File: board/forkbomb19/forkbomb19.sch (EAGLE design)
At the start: 67 parts, among them T3 MMUN2133LT1G, U1 ESP-WROOM-03, U4 TPS61090RSAR, U5 MCP73871, X3 POT_GND, X4 POT_3V3, X5 POT_SIG

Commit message: performing board review
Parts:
- TOUCH: value TOUCHPAD -> TOUCHPADTOUCH_BLANK; device forkbomb19:TOUCHPAD -> forkbomb19:TOUCHPADTOUCH_BLANK
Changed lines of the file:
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@@
 <part name="GND21" library="supply1" library_urn="urn:adsk.eagle:library:371" deviceset="GND" device=""/>
 <part name="+3V13" library="supply1" library_urn="urn:adsk.eagle:library:371" deviceset="+3V3" device=""/>
-<part name="TOUCH" library="forkbomb19" deviceset="TOUCHPAD" device=""/>
+<part name="TOUCH" library="forkbomb19" deviceset="TOUCHPAD" device="TOUCH_BLANK" value="TOUCHPADTOUCH_BLANK"/>
 <part name="U4" library="microbuilder" deviceset="VREG_TPS6103X" device="" value="TPS61090RSAR"/>
 <part name="L1" library="microbuilder" deviceset="INDUCTOR" device="TDK_VLC5045" value="6.8uH"/>
@@
 <part name="U$19" library="microbuilder" deviceset="VBAT" device=""/>
 <part name="LOW_BATT" library="led" library_urn="urn:adsk.eagle:library:259" deviceset="LED" device="CHIP-LED0603" package3d_urn="urn:adsk.eagle:package:15819/3" value="RED"/>
-<part name="R20" library="rcl" library_urn="urn:adsk.eagle:library:334" deviceset="R-US_" device="R0603" package3d_urn="urn:adsk.eagle:package:23555/2" value="1K"/>
-<part name="R18" library="rcl" library_urn="urn:adsk.eagle:library:334" deviceset="R-US_" device="R0603" package3d_urn="urn:adsk.eagle:package:23555/2" value="200K"/>
+<part name="R20" library="rcl" library_urn="urn:adsk.eagle:library:334" deviceset="R-US_" device="R0603" package3d_urn="urn:adsk.eagle:package:23555/3" value="1K"/>
+<part name="R18" library="rcl" library_urn="urn:adsk.eagle:library:334" deviceset="R-US_" device="R0603" package3d_urn="urn:adsk.eagle:package:23555/3" value="200K"/>
 <part name="U$27" library="microbuilder" deviceset="VBAT" device=""/>
 <part name="U$24" library="microbuilder" deviceset="GND" device=""/>
 <part name="C16" library="rcl" library_urn="urn:adsk.eagle:library:334" deviceset="C-US" device="C0603" package3d_urn="urn:adsk.eagle:package:23616/2" value="100nF"/>
-<part name="R19" library="rcl" library_urn="urn:adsk.eagle:library:334" deviceset="R-US_" device="R0603" package3d_urn="urn:adsk.eagle:package:23555/2" value="1.12M"/>
-<part name="R21" library="rcl" library_urn="urn:adsk.eagle:library:334" deviceset="R-US_" device="R0603" package3d_urn="urn:adsk.eagle:package:23555/2" value="200K"/>
+<part name="R19" library="rcl" library_urn="urn:adsk.eagle:library:334" deviceset="R-US_" device="R0603" package3d_urn="urn:adsk.eagle:package:23555/3" value="1.12M"/>
+<part name="R21" library="rcl" library_urn="urn:adsk.eagle:library:334" deviceset="R-US_" device="R0603" package3d_urn="urn:adsk.eagle:package:23555/3" value="200K"/>
 <part name="U$9" library="microbuilder" deviceset="GND" device=""/>
 <part name="U$10" library="microbuilder" deviceset="GND" device=""/>
-<part name="R23" library="rcl" library_urn="urn:adsk.eagle:library:334" deviceset="R-US_" device="R0603" package3d_urn="urn:adsk.eagle:package:23555/2" value="340K"/>
-<part name="R24" library="rcl" library_urn="urn:adsk.eagle:library:334" deviceset="R-US_" device="R0603" package3d_urn="urn:adsk.eagle:package:23555/2" value="1.87M"/>
+<part name="R23" library="rcl" library_urn="urn:adsk.eagle:library:334" deviceset="R-US_" device="R0603" package3d_urn="urn:adsk.eagle:package:23555/3" value="340K"/>
+<part name="R24" library="rcl" library_urn="urn:adsk.eagle:library:334" deviceset="R-US_" device="R0603" package3d_urn="urn:adsk.eagle:package:23555/3" value="1.87M"/>
 <part name="U$20" library="microbuilder" deviceset="GND" device=""/>
 <part name="U$23" library="microbuilder" deviceset="VBAT" device=""/>
 <part name="T3" library="transistor" library_urn="urn:adsk.eagle:library:402" deviceset="*-PNP_DRIVER-" device="SC59-BEC" package3d_urn="urn:adsk.eagle:package:28754/2" technology="MUN2114T1" value="MMUN2133LT1G"/>
 <part name="GND22" library="supply1" deviceset="GND" device=""/>
-<part name="R25" library="rcl" library_urn="urn:adsk.eagle:library:334" deviceset="R-US_" device="R0603" package3d_urn="urn:adsk.eagle:package:23555/2" value="270K"/>
-<part name="R26" library="rcl" library_urn="urn:adsk.eagle:library:334" deviceset="R-US_" device="R0603" package3d_urn="urn:adsk.eagle:package:23555/2" value="100K"/>
+<part name="R25" library="rcl" library_urn="urn:adsk.eagle:library:334" deviceset="R-US_" device="R0603" package3d_urn="urn:adsk.eagle:package:23555/3" value="270K"/>
+<part name="R26" library="rcl" library_urn="urn:adsk.eagle:library:334" deviceset="R-US_" device="R0603" package3d_urn="urn:adsk.eagle:package:23555/3" value="100K"/>
 <part name="GND24" library="supply1" deviceset="GND" device=""/>
 <part name="DONE" library="led" library_urn="urn:adsk.eagle:library:259" deviceset="LED" device="CHIP-LED0603" package3d_urn="urn:adsk.eagle:package:15819/3" value="GREEN"/>
 <part name="CHRG" library="led" library_urn="urn:adsk.eagle:library:259" deviceset="LED" device="CHIP-LED0603" package3d_urn="urn:adsk.eagle:package:15819/3" value="ORANGE"/>
-<part name="R27" library="rcl" library_urn="urn:adsk.eagle:library:334" deviceset="R-US_" device="R0603" package3d_urn="urn:adsk.eagle:package:23555/2" value="1K"/>
-<part name="R28" library="rcl" library_urn="urn:adsk.eagle:library:334" deviceset="R-US_" device="R0603" package3d_urn="urn:adsk.eagle:package:23555/2" value="1K"/>
+<part name="R27" library="rcl" library_urn="urn:adsk.eagle:library:334" deviceset="R-US_" device="R0603" package3d_urn="urn:adsk.eagle:package:23555/3" value="1K"/>
+<part name="R28" library="rcl" library_urn="urn:adsk.eagle:library:334" deviceset="R-US_" device="R0603" package3d_urn="urn:adsk.eagle:package:23555/3" value="1K"/>
 <part name="GND25" library="supply1" deviceset="GND" device=""/>
-<part name="R29" library="rcl" library_urn="urn:adsk.eagle:library:334" deviceset="R-US_" device="R0603" package3d_urn="urn:adsk.eagle:package:23555/2" value="1.0K"/>
-<part name="R30" library="rcl" library_urn="urn:adsk.eagle:library:334" deviceset="R-US_" device="R0603" package3d_urn="urn:adsk.eagle:package:23555/2" value="100K"/>
+<part name="R29" library="rcl" library_urn="urn:adsk.eagle:library:334" deviceset="R-US_" device="R0603" package3d_urn="urn:adsk.eagle:package:23555/3" value="1.0K"/>
+<part name="R30" library="rcl" library_urn="urn:adsk.eagle:library:334" deviceset="R-US_" device="R0603" package3d_urn="urn:adsk.eagle:package:23555/3" value="100K"/>
 <part name="GND26" library="supply1" deviceset="GND" device=""/>
 <part name="GND27" library="supply1" deviceset="GND" device=""/>
 <part name="GND29" library="supply1" deviceset="GND" device=""/>
-<part name="THERM" library="rcl" library_urn="urn:adsk.eagle:library:334" deviceset="R-US_" device="R0603" package3d_urn="urn:adsk.eagle:package:23555/2" value="15K"/>
+<part name="THERM" library="rcl" library_urn="urn:adsk.eagle:library:334" deviceset="R-US_" device="R0603" package3d_urn="urn:adsk.eagle:package:23555/3" value="15K"/>
 <part name="U$34" library="microbuilder" deviceset="VBAT" device=""/>
 <part name="U$36" library="microbuilder" deviceset="VBUS" device=""/>
@@
 <part name="U5" library="microbuilder" deviceset="MCP73871" device="" value="MCP73871"/>
 <part name="+3V11" library="supply1" library_urn="urn:adsk.eagle:library:371" deviceset="+3V3" device=""/>
-<part name="R9" library="rcl" library_urn="urn:adsk.eagle:library:334" deviceset="R-US_" device="R0603" package3d_urn="urn:adsk.eagle:package:23555/2" value="200k"/>
+<part name="R9" library="rcl" library_urn="urn:adsk.eagle:library:334" deviceset="R-US_" device="R0603" package3d_urn="urn:adsk.eagle:package:23555/3" value="200k"/>
 <part name="U$1" library="microbuilder" deviceset="GND" device=""/>
-<part name="C10" library="rcl" library_urn="urn:adsk.eagle:library:334" deviceset="CPOL-US" device="C/6032-28R" package3d_urn="urn:adsk.eagle:package:23415/1" value="100uF"/>
+<part name="C10" library="rcl" library_urn="urn:adsk.eagle:library:334" deviceset="CPOL-US" device="C/6032-28R" package3d_urn="urn:adsk.eagle:package:23415/2" value="100uF"/>
 <part name="U$7" library="forkbomb19" deviceset="MLX90640" device=""/>
 <part name="+3V14" library="supply1" library_urn="urn:adsk.eagle:library:371" deviceset="+3V3" device=""/>
@@
 <instance part="C14" gate="G$1" x="-50.8" y="-114.3" smashed="yes" rot="MR0">
 <attribute name="NAME" x="-51.816" y="-113.665" size="1.778" layer="95" rot="MR0"/>
-<attribute name="VALUE" x="-49.276" y="-121.031" size="1.778" layer="96" rot="MR0"/>
+<attribute name="VALUE" x="-49.276" y="-118.491" size="1.778" layer="96" rot="MR0"/>
 </instance>
 <instance part="GND19" gate="1" x="-50.8" y="-127" smashed="yes">
@@
 </instance>
 <instance part="C10" gate="G$1" x="-78.74" y="-101.6" smashed="yes">
-<attribute name="NAME" x="-77.724" y="-100.965" size="1.778" layer="95"/>
-<attribute name="VALUE" x="-77.724" y="-105.791" size="1.778" layer="96"/>
+<attribute name="NAME" x="-85.344" y="-100.965" size="1.778" layer="95"/>
+<attribute name="VALUE" x="-85.344" y="-105.791" size="1.778" layer="96"/>
 </instance>
 <instance part="U$7" gate="G$1" x="60.96" y="-109.22" smashed="yes"/>

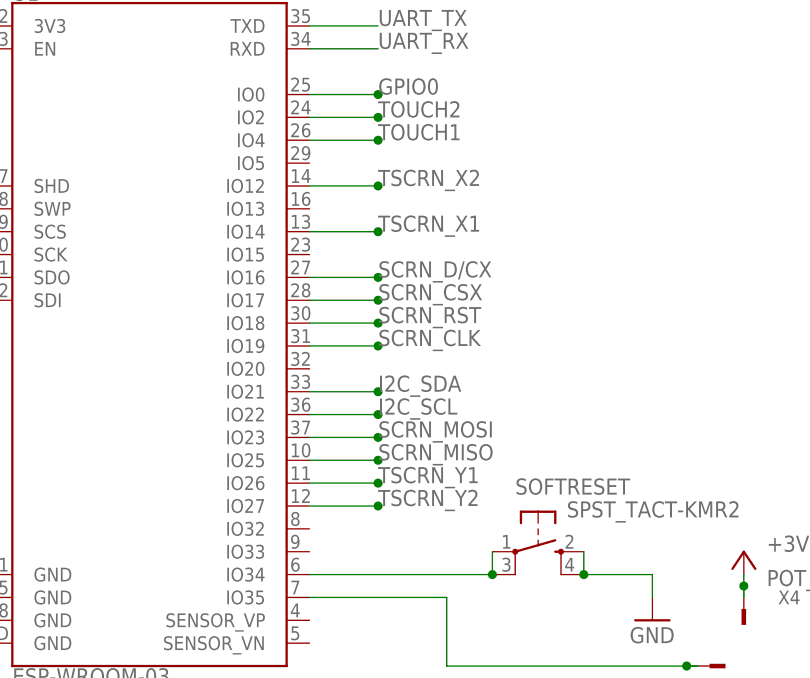
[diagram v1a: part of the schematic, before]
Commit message: TODO: Add rotary encoder, add another button, pwm the lights
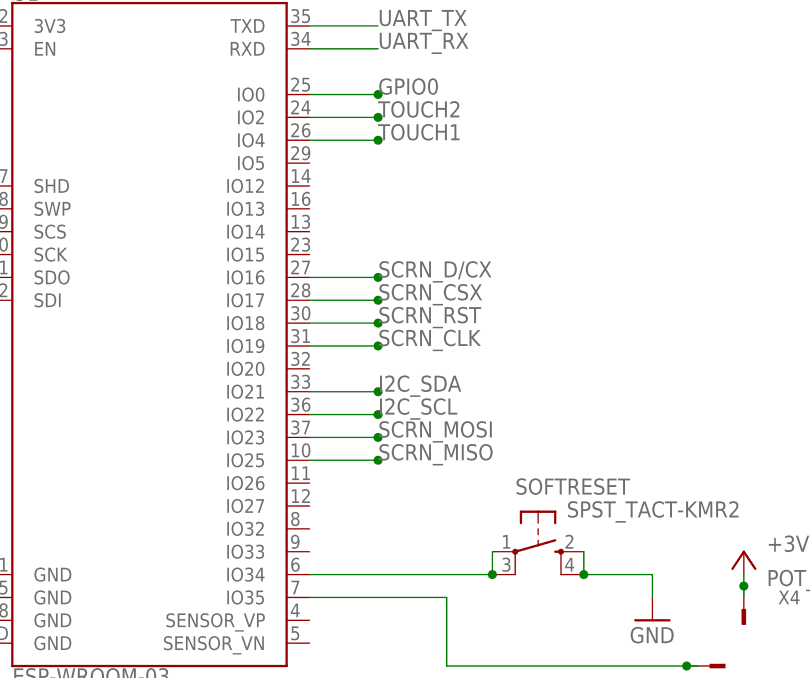
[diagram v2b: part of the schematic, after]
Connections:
- removed net TSCRN_X1: U1.IO14
- removed net TSCRN_X2: U1.IO12
- removed net TSCRN_Y1: U1.IO26
- removed net TSCRN_Y2: U1.IO27
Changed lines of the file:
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@@
-</segment>
-</net>
-<net name="TSCRN_Y2" class="0">
-<segment>
-<pinref part="U1" gate="G$1" pin="IO27"/>
-<wire x1="10.16" y1="5.08" x2="17.78" y2="5.08" width="0.1524" layer="91"/>
-<label x="17.78" y="5.08" size="1.778" layer="95"/>
-<junction x="17.78" y="5.08"/>
-</segment>
-</net>
-<net name="TSCRN_Y1" class="0">
-<segment>
-<pinref part="U1" gate="G$1" pin="IO26"/>
-<wire x1="10.16" y1="7.62" x2="17.78" y2="7.62" width="0.1524" layer="91"/>
-<label x="17.78" y="7.62" size="1.778" layer="95"/>
-<junction x="17.78" y="7.62"/>
 </segment>
 </net>
@@
 </segment>
 </net>
-<net name="TSCRN_X1" class="0">
-<segment>
-<pinref part="U1" gate="G$1" pin="IO14"/>
-<wire x1="10.16" y1="35.56" x2="17.78" y2="35.56" width="0.1524" layer="91"/>
-<label x="17.78" y="35.56" size="1.778" layer="95"/>
-<junction x="17.78" y="35.56"/>
-</segment>
-</net>
-<net name="TSCRN_X2" class="0">
-<segment>
-<pinref part="U1" gate="G$1" pin="IO12"/>
-<wire x1="10.16" y1="40.64" x2="17.78" y2="40.64" width="0.1524" layer="91"/>
-<label x="17.78" y="40.64" size="1.778" layer="95"/>
-<junction x="17.78" y="40.64"/>
-</segment>
-</net>

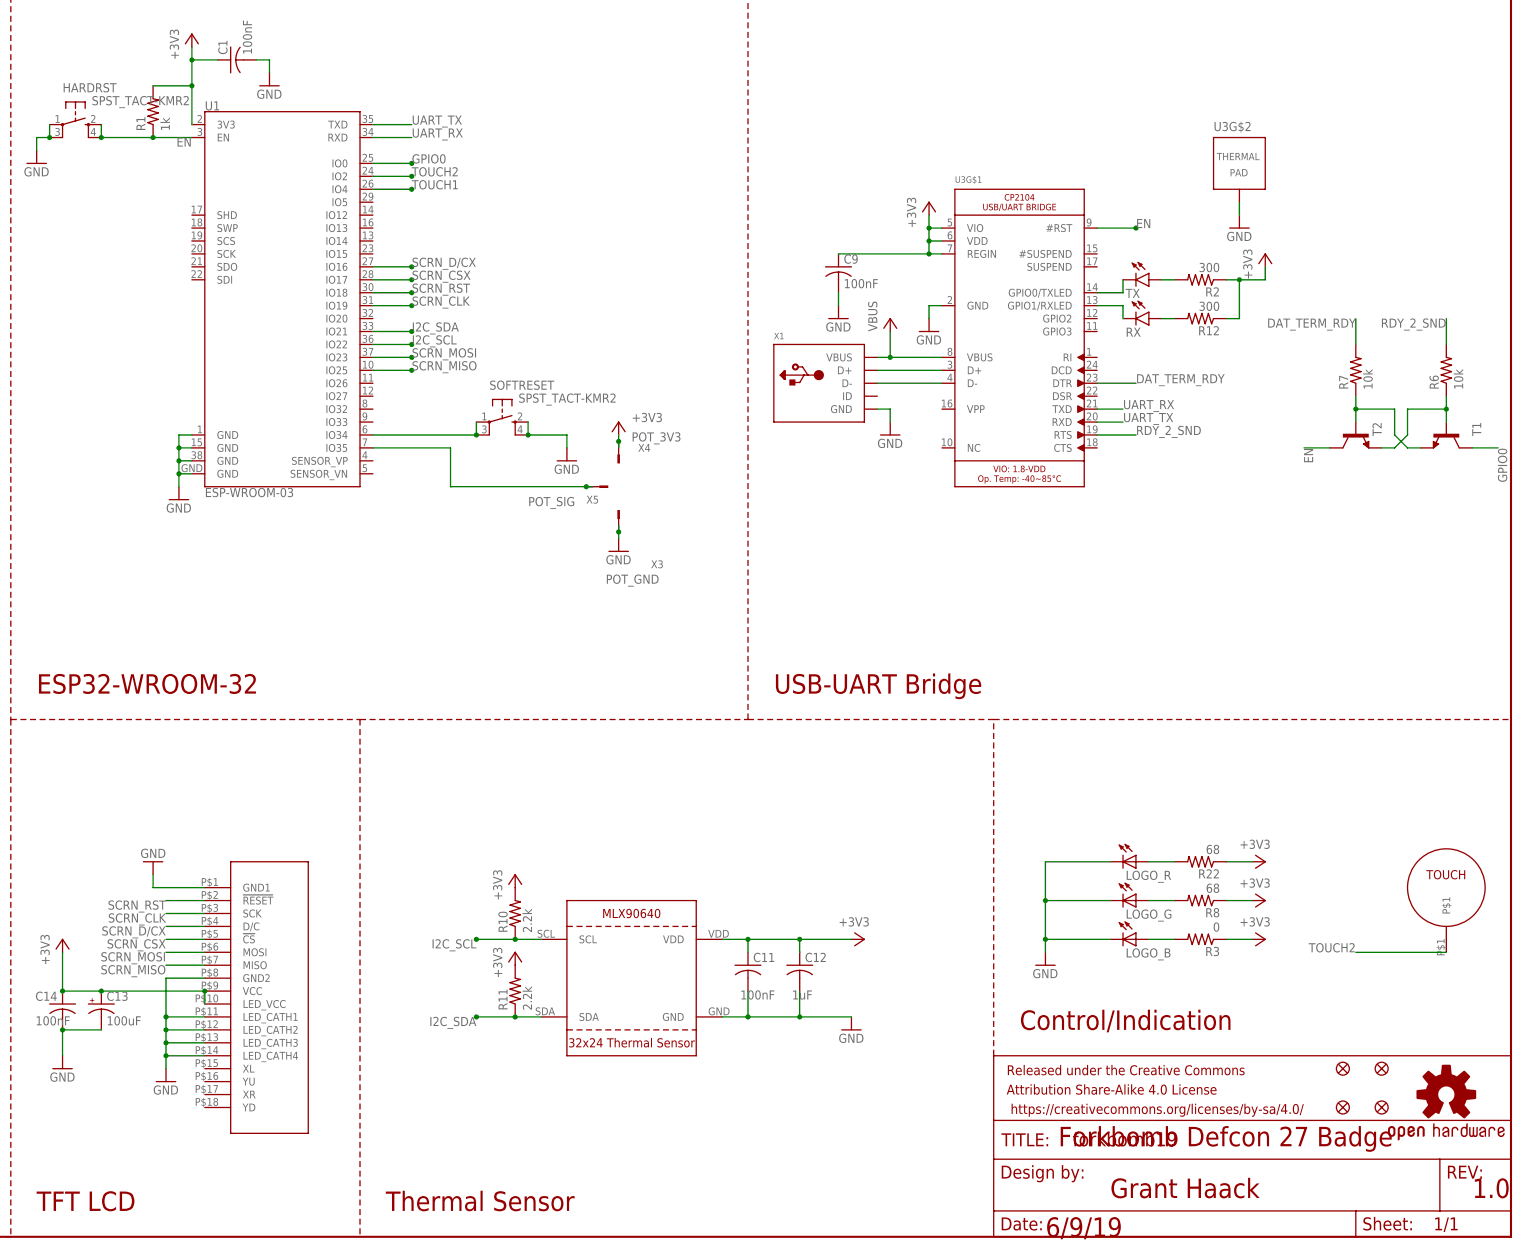
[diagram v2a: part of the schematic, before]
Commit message: added PWM control for LEDs, swapped the potentiometer for a rotary encoder, and added a menu button
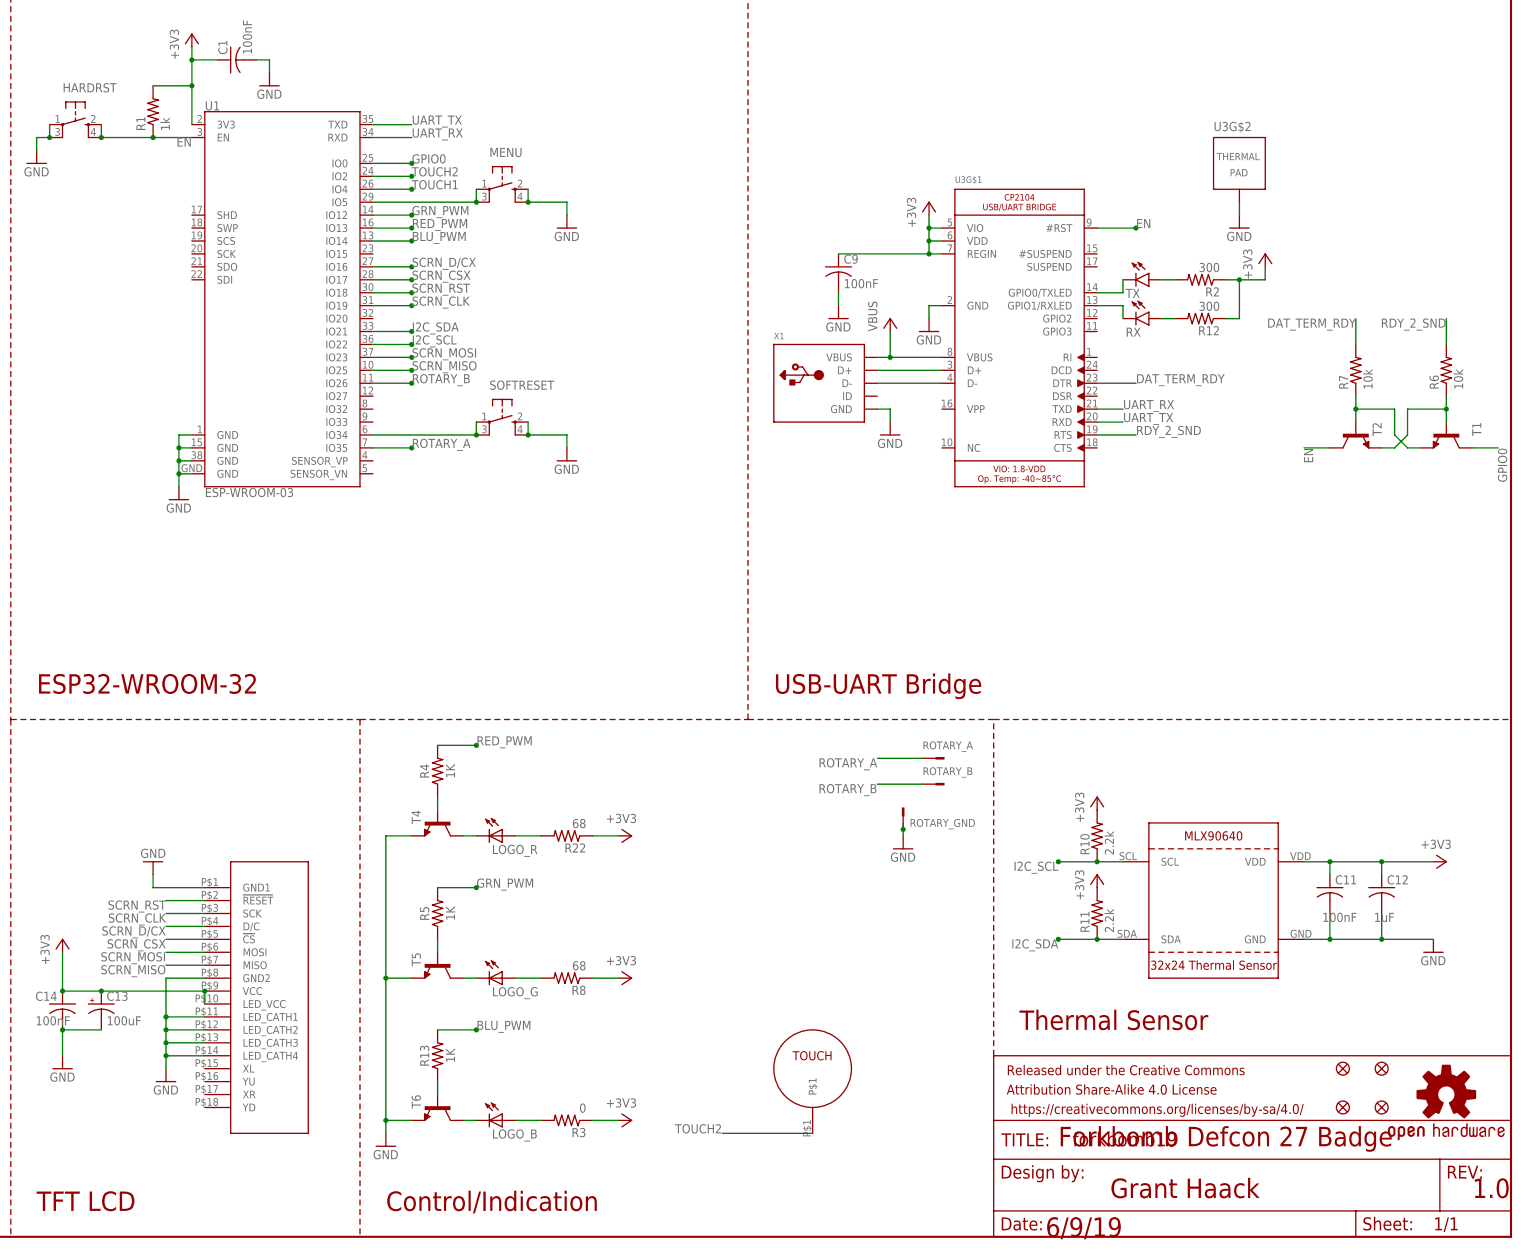
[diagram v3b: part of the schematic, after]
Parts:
- removed X3: POT_GND, con-samtec:TSW-101-07-G-S
- removed X4: POT_3V3, con-samtec:TSW-101-07-G-S
- removed X5: POT_SIG, con-samtec:TSW-101-07-G-S
- added MENU: SPST_TACT-KMR2, adafruit:SPST_TACT-KMR2
- added R13, R4, R5: 1K, rcl:R-US_R0603
- added ROTARY_A: POT_SIG, con-samtec:TSW-101-07-G-S
- added ROTARY_B: POT_3V3, con-samtec:TSW-101-07-G-S
- added ROTARY_GND: POT_GND, con-samtec:TSW-101-07-G-S
- added T4, T5, T6: (no value), transistor:MMBT3904LT1-NPN-SOT23-BEC
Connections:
- new net BLU_PWM: R13.2, U1.IO14
- new net GRN_PWM: R5.2, U1.IO12
- new net MENU: MENU.P, MENU.P1, U1.IO5
- new net N$10: R5.1, T5.B
- new net N$11: R13.1, T6.B
- new net N$14: R4.1, T4.B
- new net N$8: LOGO_G.C, T5.C
- new net N$9: LOGO_R.C, T4.C
- new net RED_PWM: R4.2, U1.IO13
- new net ROTARY_A: ROTARY_A.1, U1.IO35
- new net ROTARY_B: ROTARY_B.1, U1.IO26
- net +3V3: no longer X4.1
- net GND: now also MENU.S, MENU.S1, ROTARY_GND.1, T4.E, T5.E, T6.E; no longer LOGO_B.C, LOGO_G.C, LOGO_R.C, X3.1
- net N$4: now also LOGO_B.C, T6.C; no longer U1.IO35, X5.1
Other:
- moved on the sheet: C11, C12, LOGO_B, LOGO_G, LOGO_R, R10, R11, R22, R3, R8, TOUCH

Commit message: ready for board sign off
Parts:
- added 3V3_ROTARY: POT_GND, con-samtec:TSW-101-07-G-S
- added C3: 4.7uF, rcl:C-USC0805
- added TP_BATT_GND, TP_BATT_VBAT, TP_BATT_VLIPO, TP_I2C_GND, TP_I2C_SCL, TP_I2C_SDA, TP_PWR_3V3, TP_PWR_GND, TP_PWR_VBUS: TPSTP20SQ, testpad:TPSTP20SQ
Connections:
- net TOUCH1 renamed TOUCH0
- new net I2C_GND: TP_I2C_GND.PP
- new net VPP: C3.1, U3G$1.VPP
- net +3V3: now also 3V3_ROTARY.1, TP_PWR_3V3.PP
- net GND: now also C3.2, TP_BATT_GND.PP, TP_PWR_GND.PP
- net I2C_SCL: now also TP_I2C_SCL.PP
- net I2C_SDA: now also TP_I2C_SDA.PP
- net VBAT: now also TP_BATT_VBAT.PP
- net VBUS: now also TP_PWR_VBUS.PP
- net VLIPO: now also TP_BATT_VLIPO.PP
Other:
- note added: "LED Logo Lights"
- note added: "Rotary Encoder"
- note added: "Test Points"
- note added: "Touch Pad"
- moved on the sheet: C1, C9, HARDRST, MENU, R1, R12, R2, R6, R7, ROTARY_A, ROTARY_B, ROTARY_GND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
